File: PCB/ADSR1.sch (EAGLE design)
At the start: 48 parts, among them IC1 78L05, IC2 4066D, IC3 MCP6002, IC4 TL072D, SW1 TL2285, T1 BC847

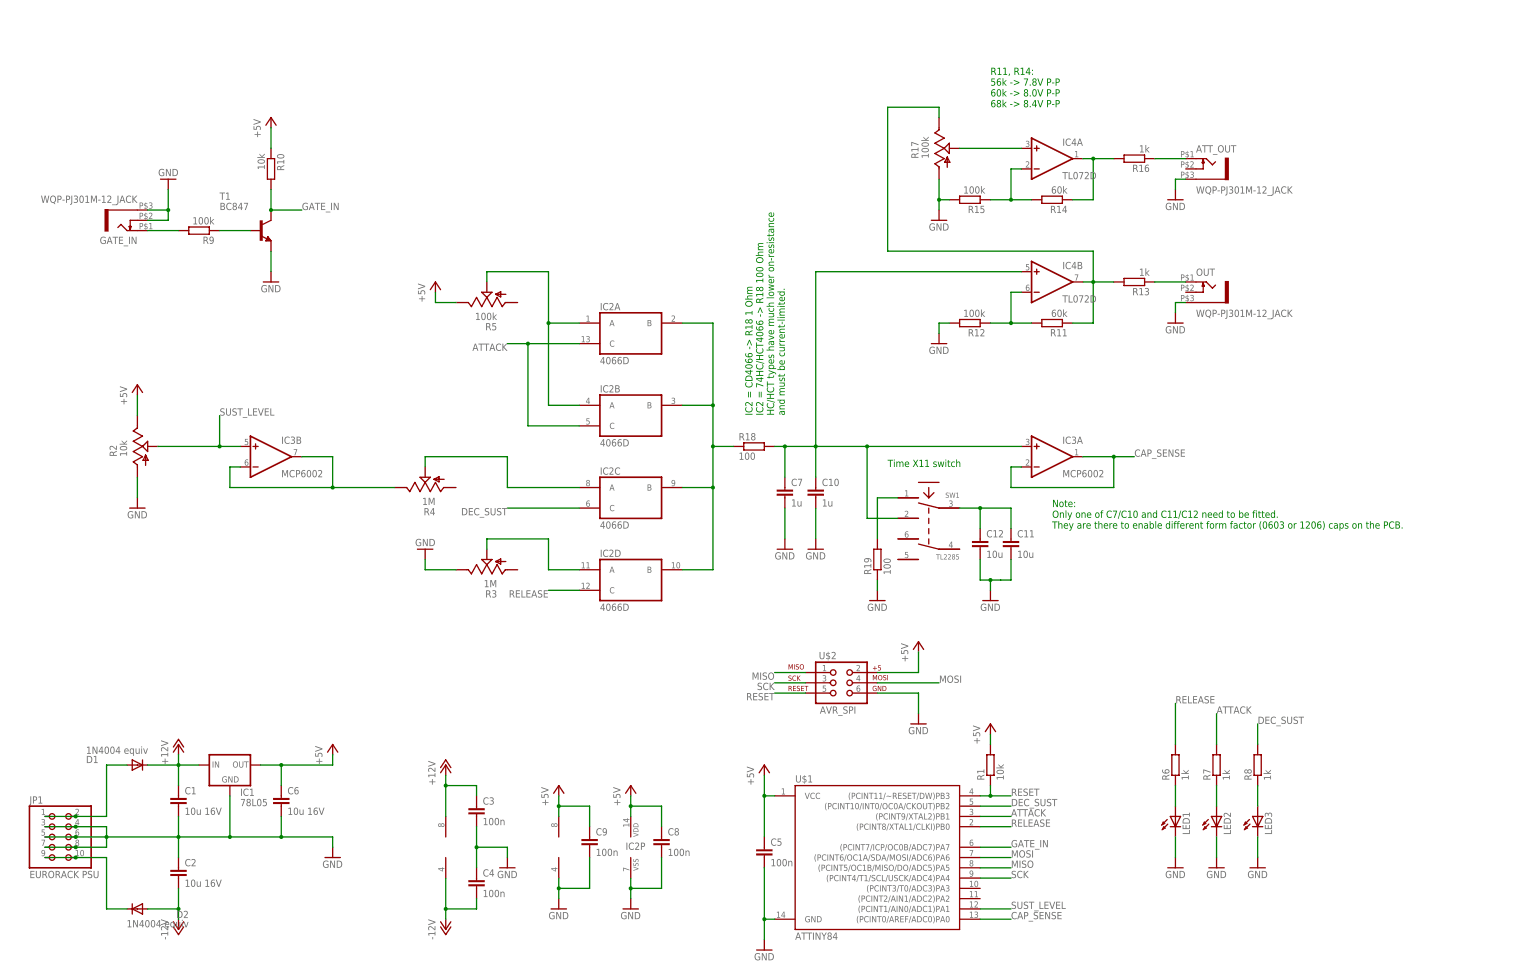
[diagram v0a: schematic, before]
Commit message: More or less working breadboard prototype. Will probably not do more with this in a while (if ever).
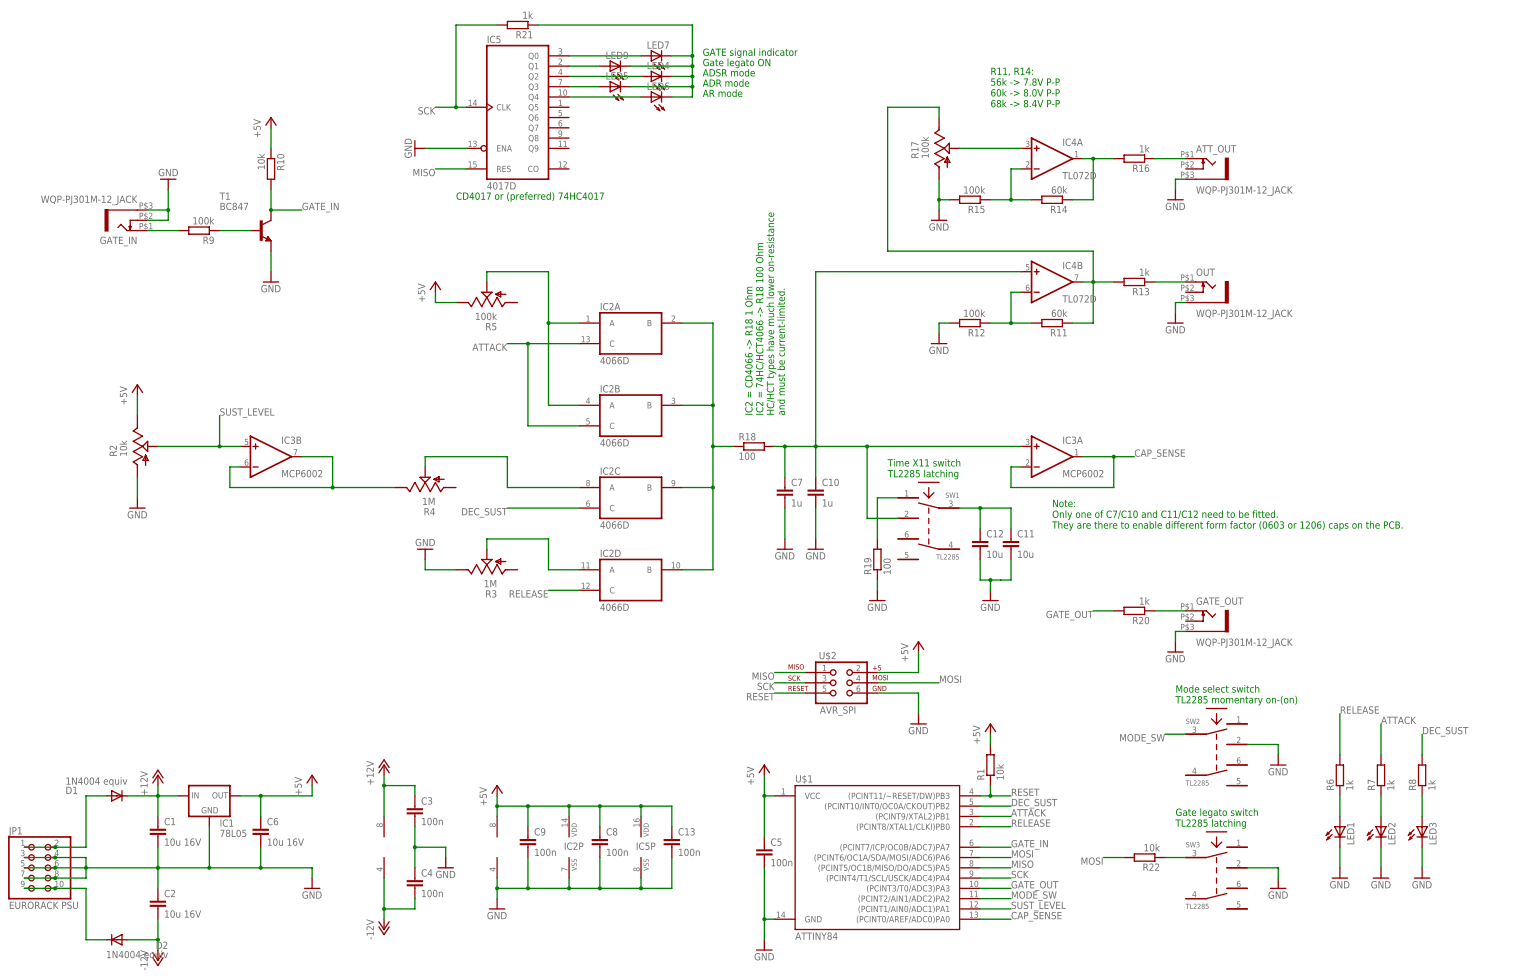
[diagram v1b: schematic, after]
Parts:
- added C13: 100n, rcl:C-EUC0603K
- added GATE_OUT: WQP-PJ301M-12_JACK, thonkiconn:WQP-PJ301M-12_JACK
- added IC5: 4017D, 40xx:4017D
- added LED4, LED5, LED6, LED7, LED9: (no value), led:LED3MM
- added R20, R21: 1k, rcl:R-EU_R0603
- added R22: 10k, rcl:R-EU_R0603
- added SW2, SW3: TL2285, lb_devs:TL2285
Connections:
- new net GATE_OUT: R20.2, U$1.(PCINT3/T0/ADC3)PA3
- new net MODE_SW: SW2.P3, U$1.(PCINT2/AIN1/ADC2)PA2
- new net N$22: IC5A.Q1, LED9.A
- new net N$23: GATE_OUT.2, R20.1
- new net N$25: IC5A.Q2, LED4.A
- new net N$26: IC5A.Q3, LED5.A
- new net N$27: IC5A.Q4, LED6.A
- new net N$28: LED4.C, LED5.C, LED6.C, LED7.C, LED9.C, R21.1
- new net N$29: IC5A.Q0, LED7.A
- new net N$30: R22.1, SW3.P3
- net +5V: now also C13.1, IC5P.VDD
- net GND: now also C13.2, GATE_OUT.1, IC5A.ENA, IC5P.VSS, SW2.P2, SW3.P2
- net MISO: now also IC5A.RES
- net MOSI: now also R22.2
- net SCK: now also IC5A.CLK, R21.2
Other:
- note added: "ADR mode"
- note added: "ADSR mode"
- note added: "AR mode"
- note added: "CD4017 or (preferred) 74HC4017"
- note added: "GATE signal indicator"
- note added: "Gate legato ON"
- note added: "Gate legato switch TL2285 latching"
- note added: "Mode select switch TL2285 momentary on-(on)"
- note added: "Time X11 switch TL2285 latching"
- note removed: "Time X11 switch"
- moved on the sheet: C1, C2, C3, C4, C6, C8, C9, D1, D2, IC1, IC2P, JP1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
